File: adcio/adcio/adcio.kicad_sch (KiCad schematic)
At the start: 4 parts, among them J3 RJ45_Shielded, J4 RJ45_Shielded

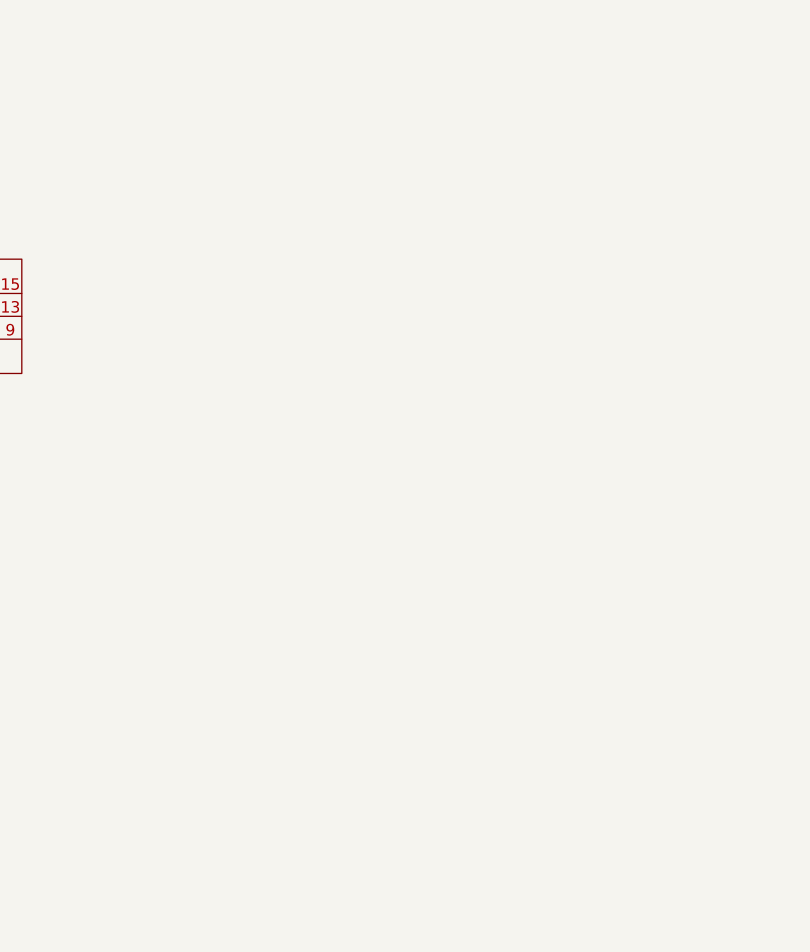
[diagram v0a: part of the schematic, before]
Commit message: Added level shifters.
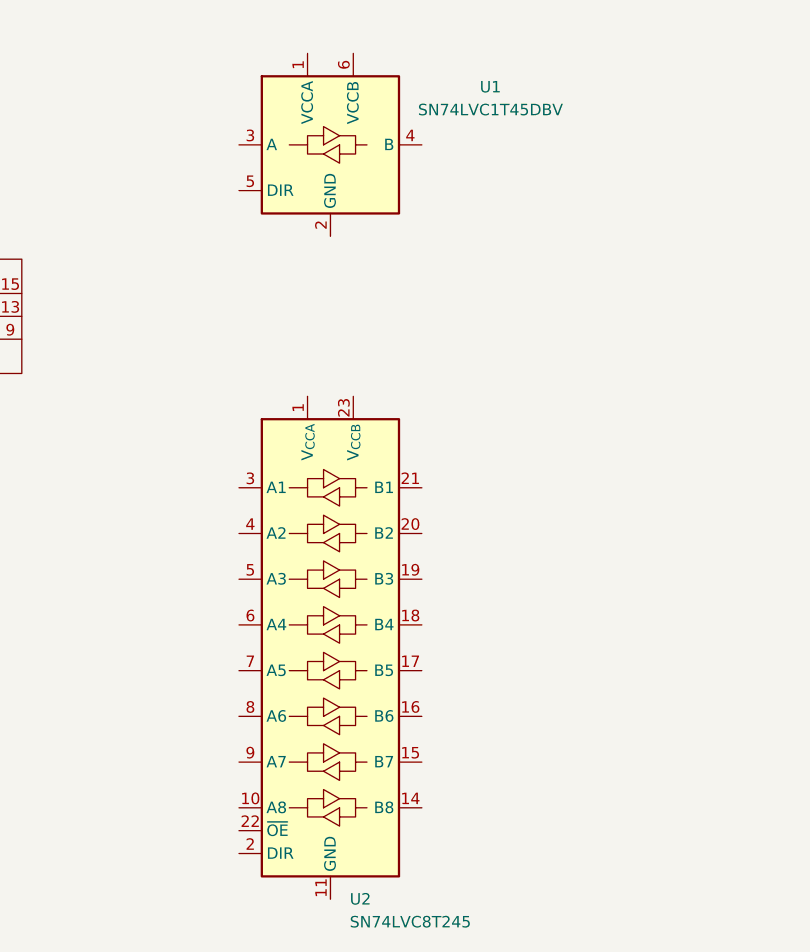
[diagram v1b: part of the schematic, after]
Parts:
- added U1: SN74LVC1T45DBV, Package_TO_SOT_SMD:SOT-23-6, symbol Logic_LevelTranslator:SN74LVC1T45DBV
- added U2: SN74LVC8T245, Package_SO:TSSOP-24_4.4x7.8mm_P0.65mm, symbol Logic_LevelTranslator:SN74LVC8T245
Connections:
- new net: U2.11 (GND), U2.12 (GND), U2.13 (GND)
- new net: U2.23 (V_{CCB}), U2.24 (V_{CCB})
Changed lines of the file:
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@@
+	)
+	(symbol
+		(lib_id "Logic_LevelTranslator:SN74LVC1T45DBV")
+		(at 99.06 55.88 0)
+		(unit 1)
+		(body_style 1)
+		(exclude_from_sim no)
+		(in_bom yes)
+		(on_board yes)
+		(in_pos_files yes)
+		(dnp no)
+		(fields_autoplaced yes)
+		(property "Reference" "U1"
+			(at 116.84 49.4598 0)
+			(show_name no)
+			(do_not_autoplace no)
+			(effects
+				(font
+					(size 1.27 1.27)
+				)
+			)
+		)
+		(property "Value" "SN74LVC1T45DBV"
+			(at 116.84 51.9998 0)
+			(show_name no)
+			(do_not_autoplace no)
+			(effects
+				(font
+					(size 1.27 1.27)
+				)
+			)
+		)
+		(property "Footprint" "Package_TO_SOT_SMD:SOT-23-6"
+			(at 99.06 67.31 0)
+			(hide yes)
+			(show_name no)
+			(do_not_autoplace no)
+			(effects
+				(font
+					(size 1.27 1.27)
+				)
+			)
+		)
+		(property "Datasheet" "http://www.ti.com/lit/ds/symlink/sn74lvc1t45.pdf"
+			(at 76.2 72.39 0)
+			(hide yes)
+			(show_name no)
+			(do_not_autoplace no)
+			(effects
+				(font
+					(size 1.27 1.27)
+				)
+			)
+		)
+		(property "Description" "Single-Bit Dual-Supply Bus Transceiver With Configurable Voltage Translation and 3-State Outputs, SOT-23-6"
+			(at 99.06 55.88 0)
+			(hide yes)
+			(show_name no)
+			(do_not_autoplace no)
+			(effects
+				(font
+					(size 1.27 1.27)
+				)
+			)
+		)
+		(pin "5"
+		)
+		(pin "4"
+		)
+		(pin "2"
+		)
+		(pin "3"
+		)
+		(pin "1"
+		)
+		(pin "6"
+		)
+		(instances
+			(project "adcio"
+				(path "/5e5d26d6-6f87-474c-8bed-bf7a7546c8ba"
+					(reference "U1")
+					(unit 1)
+				)
+			)
+		)
 	)
 	(symbol
@@
 					(unit 1)
 				)
+			)
+		)
+	)
+	(symbol
+		(lib_id "Logic_LevelTranslator:SN74LVC8T245")
+		(at 99.06 111.76 0)
+		(unit 1)
+		(body_style 1)
+		(exclude_from_sim no)
+		(in_bom yes)
+		(on_board yes)
+		(in_pos_files yes)
+		(dnp no)
+		(fields_autoplaced yes)
+		(property "Reference" "U2"
+			(at 101.2033 139.7 0)
+			(show_name no)
+			(do_not_autoplace no)
+			(effects
+				(font
+					(size 1.27 1.27)
+				)
+				(justify left)
+			)
+		)
+		(property "Value" "SN74LVC8T245"
+			(at 101.2033 142.24 0)
+			(show_name no)
+			(do_not_autoplace no)
+			(effects
+				(font
+					(size 1.27 1.27)
+				)
+				(justify left)
+			)
+		)
+		(property "Footprint" "Package_SO:TSSOP-24_4.4x7.8mm_P0.65mm"
+			(at 119.38 135.89 0)
+			(hide yes)
+			(show_name no)
+			(do_not_autoplace no)
+			(effects
+				(font
+					(size 1.27 1.27)
+				)
+			)
+		)
+		(property "Datasheet" "https://www.ti.com/lit/ds/symlink/sn74lvc8t245.pdf"
+			(at 99.06 147.32 0)
+			(hide yes)
+			(show_name no)
+			(do_not_autoplace no)
+			(effects
+				(font
+					(size 1.27 1.27)
+				)
+			)
+		)
+		(property "Description" "8-Bit Dual-Supply Bus Transceiver With Configurable Voltage Translation and 3-State Outputs"
+			(at 99.06 111.76 0)
+			(hide yes)
+			(show_name no)
+			(do_not_autoplace no)
+			(effects
+				(font
+					(size 1.27 1.27)
+				)
+			)
+		)
+		(pin "2"
+		)
+		(pin "8"
+		)
+		(pin "10"
+		)
+		(pin "14"
+		)
+		(pin "6"
+		)
+		(pin "17"
+		)
+		(pin "4"
+		)
+		(pin "11"
+		)
+		(pin "7"
+		)
+		(pin "3"
+		)
+		(pin "5"
+		)
+		(pin "12"
+		)
+		(pin "1"
+		)
+		(pin "9"
+		)
+		(pin "13"
+		)
+		(pin "15"
+		)
+		(pin "16"
+		)
+		(pin "22"
+		)
+		(pin "19"
+		)
+		(pin "24"
+		)
+		(pin "23"
+		)
+		(pin "20"
+		)
+		(pin "21"
+		)
+		(pin "18"
+		)
+		(instances
+			(project "adcio"
+				(path "/5e5d26d6-6f87-474c-8bed-bf7a7546c8ba"
+					(reference "U2")
+					(unit 1)
+				)

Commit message: ADCIO PCB done.
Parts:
- added C1, C10, C11, C12, C13, C14, C15, C16, C17, C18, C19, C2, C20, C21, C22, C23, C24, C3, C4, C5, C6, C7, C8, C9: 100n, Capacitor_SMD:C_0805_2012Metric_Pad1.18x1.45mm_HandSolder, symbol Device:C
- added U10, U11: MAX3232, Package_SO:SSOP-16_5.3x6.2mm_P0.65mm, symbol Interface_UART:MAX3232
- added U12: 74LS32, Package_SO:SOIC-14_3.9x8.7mm_P1.27mm, symbol 74xx:74LS32
- added U13: 74LS00, Package_SO:SOIC-14_3.9x8.7mm_P1.27mm, symbol 74xx:74LS00
- added U3: TLV70018_SOT353, Package_TO_SOT_SMD:SOT-353_SC-70-5, symbol Regulator_Linear:TLV70018_SOT353
- added U4, U5, U6, U7, U8, U9: MAX3485, Package_SO:SOIC-8_3.9x4.9mm_P1.27mm, symbol Interface_UART:MAX3485
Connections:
- net 3.3v: now also U1.6 (VCCB), U2.23 (V_{CCB}), U2.24 (V_{CCB}), C1.1, C11.1, C12.1, C13.1, C14.1, C15.1, C16.1, C17.1, C18.1, C19.1, C20.1, C21.1, C22.1, U10.16 (VCC), U11.16 (VCC), U12.14 (VCC), U13.14 (VCC), U3.1 (IN), U3.3 (EN), U4.2 (~{RE}), U4.3 (DE), U4.8 (VCC), U5.8 (VCC), U6.2 (~{RE}), U6.3 (DE), U6.8 (VCC), U7.2 (~{RE}), U7.3 (DE), U7.8 (VCC), U8.8 (VCC), U9.2 (~{RE}), U9.3 (DE), U9.8 (VCC)
- net GND: now also J3.SH, J4.SH, U1.2 (GND), U2.10 (A8), U2.11 (GND), U2.12 (GND), U2.13 (GND), U2.22 (~{OE}), U2.8 (A6), U2.9 (A7), C1.2, C10.2, C11.2, C12.2, C13.2, C14.2, C15.2, C16.2, C17.2, C18.2, C19.2, C2.2, C20.2, C21.2, C22.2, C23.2, C24.2, C7.2, C8.2, C9.2, U10.13 (R1IN), U10.15 (GND), U10.8 (R2IN), U11.13 (R1IN), U11.15 (GND), U11.8 (R2IN), U12.7 (GND), U13.7 (GND), U3.2 (GND), U4.5 (GND), U5.2 (~{RE}), U5.3 (DE), U5.4 (DI), U5.5 (GND), U6.5 (GND), U7.5 (GND), U8.2 (~{RE}), U8.3 (DE), U8.4 (DI), U8.5 (GND), U9.5 (GND)
- net at J2.1 (CLK): now also U2.6 (A4)
- net at J2.13 (CS1): now also U2.4 (A2)
- net at J2.15 (CS2): now also U2.5 (A3)
- net at J2.3 (DIN): now also U2.7 (A5)
- net at J2.7 (DOUT): now also U1.3 (A)
- net at J2.9 (CS0): now also U2.3 (A1)
- net at J4.1: now also U7.6 (A)
- net at J4.2: now also U7.7 (B)
- net at J4.3: now also U8.6 (A)
- net at J4.4: now also U9.6 (A)
- net at J4.5: now also U9.7 (B)
- net at J4.6: now also U8.7 (B)
- net at J4.7: now also U11.14 (T1OUT)
- net at J4.8: now also U11.7 (T2OUT)
- net 1.8v: now reaches U1.1 (VCCA)
- net 1.8v: now also U2.1 (V_{CCA}), U2.2 (DIR), C2.1, C23.1, C24.1, U3.5 (OUT)
- net at U1.4 (B): now also U13.11
- net at J3.1: now also U4.6 (A)
- net at J3.2: now also U4.7 (B)
- net at J3.3: now also U5.6 (A)
- net at J3.4: now also U6.6 (A)
- net at J3.5: now also U6.7 (B)
- net at J3.6: now also U5.7 (B)
- net at J3.7: now also U10.14 (T1OUT)
- net at J3.8: now also U10.7 (T2OUT)
- net SPI_OUT: now reaches U2.17 (B5)
- net SPI_OUT: now also U6.4 (DI), U9.4 (DI)
- net SPI_CLK: now reaches U2.18 (B4)
- net SPI_CLK: now also U4.4 (DI), U7.4 (DI)
- net SEL2: now reaches U2.19 (B3)
- net SEL2: now also U12.10, U12.13, U13.1, U13.2, U13.9
- net SEL1: now reaches U2.20 (B2)
- net SEL1: now also U12.12, U12.4
- net SEL0: now reaches U2.21 (B1)
- net SEL0: now also U12.1, U12.9
- new net: C8.1, U10.6 (VS-)
- new net: C5.1, U11.1 (C1+)
- new net: C5.2, U11.3 (C1-)
- new net: U13.10, U8.1 (RO)
- new net: U11.10 (T2IN), U12.6
- new net: U13.13, U13.8
- new net: C10.1, U11.6 (VS-)
- new net: U13.5, U5.1 (RO)
- new net: U13.12, U13.6
- new net: C9.1, U11.2 (VS+)
- new net: C6.1, U11.4 (C2+)
- new net: C6.2, U11.5 (C2-)
- new net: U11.11 (T1IN), U12.3
- new net: C4.1, U10.4 (C2+)
- new net: C4.2, U10.5 (C2-)
- new net: U10.10 (T2IN), U12.11
- new net: C3.1, U10.1 (C1+)
- new net: U10.11 (T1IN), U12.8
- new net: C7.1, U10.2 (VS+)
- new net: C3.2, U10.3 (C1-)
- new net INV_SEL2: U12.2, U12.5, U13.3, U13.4
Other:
- moved on the sheet: J1, J2, J3, J4, U1, U2
